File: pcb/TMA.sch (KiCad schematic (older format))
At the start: 22 parts, among them J1 Conn_01x02, J2 Conn_01x06, SW1 SW_SPDT, U1 BMP280, U2 BMI160, U3 ATtiny1614-SS, U4 MIC5504-3.3YM5

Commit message: Pick components.
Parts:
- C1, C2, C3, C4, C5, C6, C7: footprint (none) -> Capacitor_SMD:C_0402_1005Metric
- D1: renamed from D?; footprint (none) -> Diode_SMD:D_0402_1005Metric
- D3, D4: footprint (none) -> LED_SMD:LED_0402_1005Metric
- J1: footprint (none) -> Connector_JST:JST_PH_B2B-PH-K_1x02_P2.00mm_Vertical
- J2: footprint (none) -> Connector_JST:JST_PH_B6B-PH-K_1x06_P2.00mm_Vertical
- R1, R2, R3, R4, R5: footprint (none) -> Resistor_SMD:R_0402_1005Metric
- SW1: footprint (none) -> Button_Switch_SMD:SW_SPDT_PCM12
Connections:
- net UPDI: now also D1.2 (A)
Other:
- moved on the sheet: D1
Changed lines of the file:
@@
 F 0 "C1" H 2092 3346 50  0000 L CNN
 F 1 "100nF" H 2092 3255 50  0000 L CNN
-F 2 "" H 2000 3300 50  0001 C CNN
+F 2 "Capacitor_SMD:C_0402_1005Metric" H 2000 3300 50  0001 C CNN
 F 3 "~" H 2000 3300 50  0001 C CNN
 	1    2000 3300
@@
 F 0 "C2" H 2242 1096 50  0000 L CNN
 F 1 "100nF" H 2242 1005 50  0000 L CNN
-F 2 "" H 2150 1050 50  0001 C CNN
+F 2 "Capacitor_SMD:C_0402_1005Metric" H 2150 1050 50  0001 C CNN
 F 3 "~" H 2150 1050 50  0001 C CNN
 	1    2150 1050
@@
 F 0 "J1" H 2818 775 50  0000 C CNN
 F 1 "Conn_01x02" H 2818 866 50  0000 C CNN
-F 2 "" H 2900 1100 50  0001 C CNN
+F 2 "Connector_JST:JST_PH_B2B-PH-K_1x02_P2.00mm_Vertical" H 2900 1100 50  0001 C CNN
 F 3 "~" H 2900 1100 50  0001 C CNN
 	1    2900 1100
@@
 F 0 "C3" H 2942 2796 50  0000 L CNN
 F 1 "100nF" H 2942 2705 50  0000 L CNN
-F 2 "" H 2850 2750 50  0001 C CNN
+F 2 "Capacitor_SMD:C_0402_1005Metric" H 2850 2750 50  0001 C CNN
 F 3 "~" H 2850 2750 50  0001 C CNN
 	1    2850 2750
@@
 F 0 "C4" H 3592 1296 50  0000 L CNN
 F 1 "4u7" H 3592 1205 50  0000 L CNN
-F 2 "" H 3500 1250 50  0001 C CNN
+F 2 "Capacitor_SMD:C_0402_1005Metric" H 3500 1250 50  0001 C CNN
 F 3 "~" H 3500 1250 50  0001 C CNN
 	1    3500 1250
@@
 F 0 "C5" H 4042 1296 50  0000 L CNN
 F 1 "100nF" H 4042 1205 50  0000 L CNN
-F 2 "" H 3950 1250 50  0001 C CNN
+F 2 "Capacitor_SMD:C_0402_1005Metric" H 3950 1250 50  0001 C CNN
 F 3 "~" H 3950 1250 50  0001 C CNN
 	1    3950 1250
@@
 $EndComp
 Connection ~ 3950 1000
-Wire Wire Line
-	3950 1000 4300 1000
 $Comp
 L power:GND #PWR09
@@
 F 0 "C6" H 5642 1296 50  0000 L CNN
 F 1 "4u7" H 5642 1205 50  0000 L CNN
-F 2 "" H 5550 1250 50  0001 C CNN
+F 2 "Capacitor_SMD:C_0402_1005Metric" H 5550 1250 50  0001 C CNN
 F 3 "~" H 5550 1250 50  0001 C CNN
 	1    5550 1250
@@
 F 0 "C7" H 6092 1296 50  0000 L CNN
 F 1 "100nF" H 6092 1205 50  0000 L CNN
-F 2 "" H 6000 1250 50  0001 C CNN
+F 2 "Capacitor_SMD:C_0402_1005Metric" H 6000 1250 50  0001 C CNN
 F 3 "~" H 6000 1250 50  0001 C CNN
 	1    6000 1250
@@
 Wire Wire Line
 	4750 1500 4750 1450
-Wire Wire Line
-	4300 1000 4300 1200
-Wire Wire Line
-	4300 1200 4350 1200
-Connection ~ 4300 1000
-Wire Wire Line
-	4300 1000 4350 1000
 $Comp
 L power:+3.3V #PWR010
@@
 F 0 "R1" V 7454 1050 50  0000 C CNN
 F 1 "5k" V 7545 1050 50  0000 C CNN
-F 2 "" H 7650 1050 50  0001 C CNN
+F 2 "Resistor_SMD:R_0402_1005Metric" H 7650 1050 50  0001 C CNN
 F 3 "~" H 7650 1050 50  0001 C CNN
 	1    7650 1050
@@
 F 0 "J2" H 6868 725 50  0000 C CNN
 F 1 "Conn_01x06" H 6868 816 50  0000 C CNN
-F 2 "" H 6950 1250 50  0001 C CNN
+F 2 "Connector_JST:JST_PH_B6B-PH-K_1x06_P2.00mm_Vertical" H 6950 1250 50  0001 C CNN
 F 3 "~" H 6950 1250 50  0001 C CNN
 	1    6950 1250
@@
 F 0 "D3" V 8696 1030 50  0000 R CNN
 F 1 "BLUE" V 8605 1030 50  0000 R CNN
-F 2 "" V 8650 1100 50  0001 C CNN
+F 2 "LED_SMD:LED_0402_1005Metric" V 8650 1100 50  0001 C CNN
 F 3 "~" V 8650 1100 50  0001 C CNN
 	1    8650 1100
@@
 F 0 "D4" V 9496 1030 50  0000 R CNN
 F 1 "RED" V 9405 1030 50  0000 R CNN
-F 2 "" V 9450 1100 50  0001 C CNN
+F 2 "LED_SMD:LED_0402_1005Metric" V 9450 1100 50  0001 C CNN
 F 3 "~" V 9450 1100 50  0001 C CNN
 	1    9450 1100
@@
 F 0 "R2" H 8500 1300 50  0000 C CNN
 F 1 "10k" H 8500 1400 50  0000 C CNN
-F 2 "" H 8650 1350 50  0001 C CNN
+F 2 "Resistor_SMD:R_0402_1005Metric" H 8650 1350 50  0001 C CNN
 F 3 "~" H 8650 1350 50  0001 C CNN
 	1    8650 1350
@@
 F 0 "R3" H 9300 1300 50  0000 C CNN
 F 1 "10k" H 9300 1400 50  0000 C CNN
-F 2 "" H 9450 1350 50  0001 C CNN
+F 2 "Resistor_SMD:R_0402_1005Metric" H 9450 1350 50  0001 C CNN
 F 3 "~" H 9450 1350 50  0001 C CNN
 	1    9450 1350
@@
 F 0 "R4" V 10400 900 50  0000 C CNN
 F 1 "10k" V 10400 1050 50  0000 C CNN
-F 2 "" H 10500 1000 50  0001 C CNN
+F 2 "Resistor_SMD:R_0402_1005Metric" H 10500 1000 50  0001 C CNN
 F 3 "~" H 10500 1000 50  0001 C CNN
 	1    10500 1000
@@
 F 0 "R5" V 10400 700 50  0000 C CNN
 F 1 "10k" V 10400 850 50  0000 C CNN
-F 2 "" H 10500 800 50  0001 C CNN
+F 2 "Resistor_SMD:R_0402_1005Metric" H 10500 800 50  0001 C CNN
 F 3 "~" H 10500 800 50  0001 C CNN
 	1    10500 800
@@
 F 0 "SW1" H 10350 1350 50  0000 C CNN
 F 1 "SW_SPDT" H 10350 1450 50  0000 C CNN
-F 2 "" H 10550 1600 50  0001 C CNN
+F 2 "Button_Switch_SMD:SW_SPDT_PCM12" H 10550 1600 50  0001 C CNN
 F 3 "~" H 10550 1600 50  0001 C CNN
 	1    10550 1600
@@
 MODE
 Wire Wire Line
-	7800 1050 8000 1050
+	7800 1050 7900 1050
 Wire Wire Line
 	10600 800  10700 800
@@
 Connection ~ 10700 800
 $Comp
-L power:+3.3V #PWR?
+L power:+3.3V #PWR0107
 U 1 1 607905AF
-P 7900 700
-F 0 "#PWR?" H 7900 550 50  0001 C CNN
-F 1 "+3.3V" H 8100 800 50  0000 C CNN
-F 2 "" H 7900 700 50  0001 C CNN
-F 3 "" H 7900 700 50  0001 C CNN
-	1    7900 700
-	1    0    0    -1
-$EndComp
-$Comp
-L Device:D_Schottky D?
+P 7900 650
+F 0 "#PWR0107" H 7900 500 50  0001 C CNN
+F 1 "+3.3V" H 8100 750 50  0000 C CNN
+F 2 "" H 7900 650 50  0001 C CNN
+F 3 "" H 7900 650 50  0001 C CNN
+	1    7900 650
+	1    0    0    -1
+$EndComp
+$Comp
+L Device:D_Schottky D1
 U 1 1 607905B5
-P 7900 900
-F 0 "D?" V 7800 1050 50  0000 C CNN
-F 1 "D_Schottky" V 7900 1200 50  0000 C CNN
-F 2 "" H 7900 900 50  0001 C CNN
-F 3 "~" H 7900 900 50  0001 C CNN
-	1    7900 900
-	0    1    1    0
-$EndComp
-Wire Wire Line
-	7900 750  7900 700
+P 7900 850
+F 0 "D1" V 7800 1000 50  0000 C CNN
+F 1 "D_Schottky" V 7900 1150 50  0000 C CNN
+F 2 "Diode_SMD:D_0402_1005Metric" H 7900 850 50  0001 C CNN
+F 3 "~" H 7900 850 50  0001 C CNN
+	1    7900 850
+	0    1    1    0
+$EndComp
+Wire Wire Line
+	7900 700  7900 650
 Wire Notes Line
 	5400 4650 5400 1850
@@
 Wire Wire Line
 	6000 1000 6100 1000
+Wire Wire Line
+	7900 1050 7900 1000
+Connection ~ 7900 1050
+Wire Wire Line
+	7900 1050 8000 1050
+Wire Wire Line
+	3950 1000 4300 1000
+Wire Wire Line
+	4350 1200 4300 1200
+Wire Wire Line
+	4300 1200 4300 1000
+Connection ~ 4300 1000
+Wire Wire Line
+	4300 1000 4350 1000
 $EndSCHEMATC

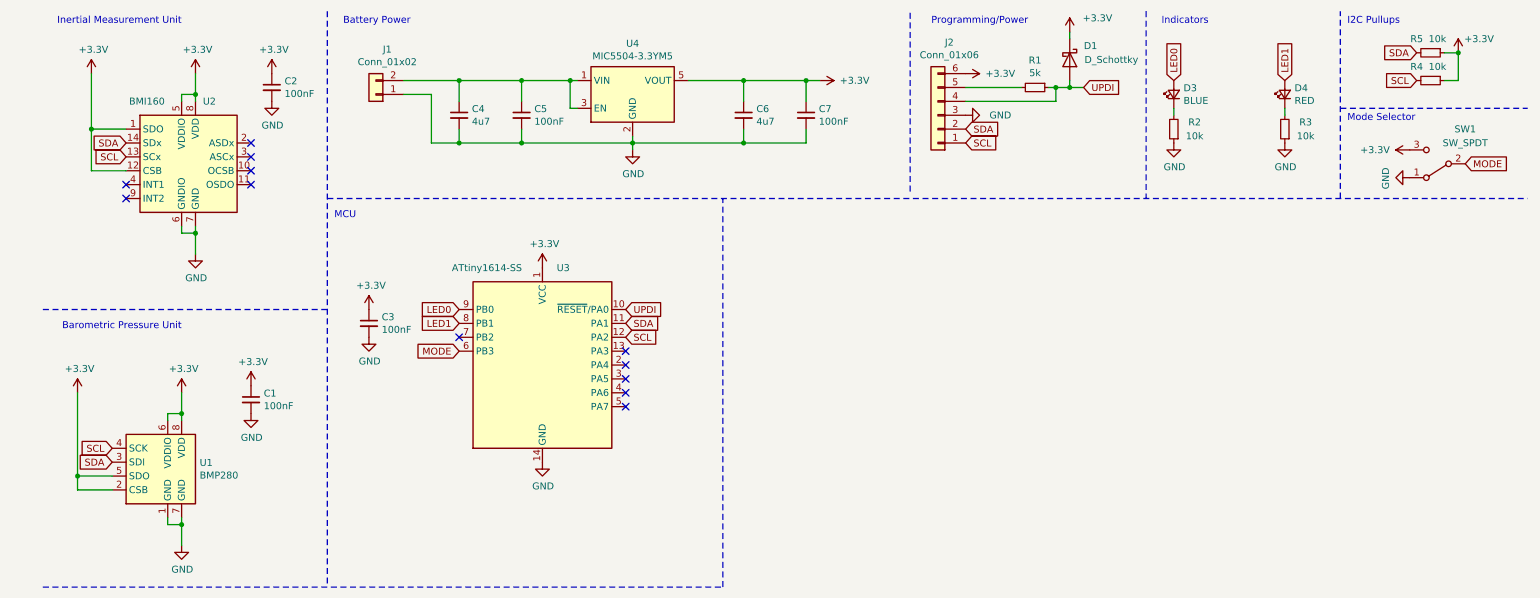
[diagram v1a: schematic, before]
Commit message: Serial, simplify programmer (trust it), break out I2C.
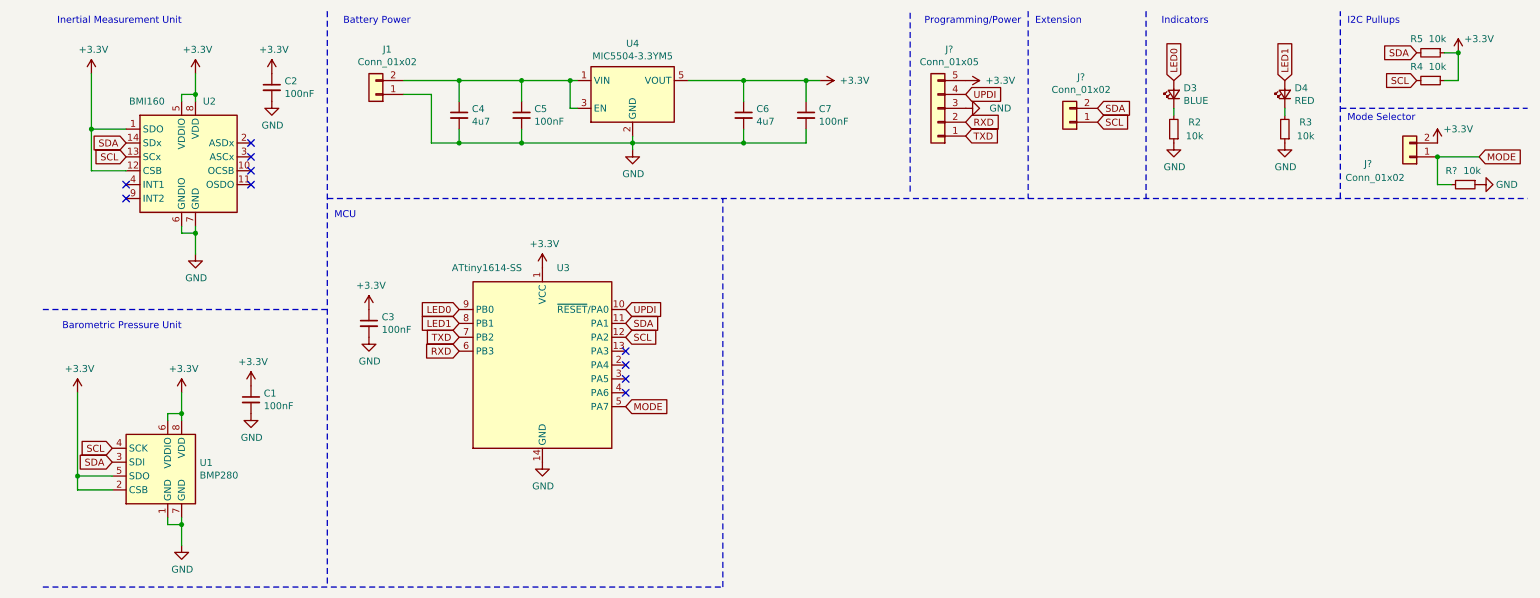
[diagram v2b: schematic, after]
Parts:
- removed D1: D_Schottky, Diode_SMD:D_0402_1005Metric, symbol Device:D_Schottky
- removed J2: Conn_01x06, Connector_JST:JST_PH_B6B-PH-K_1x06_P2.00mm_Vertical, symbol Connector_Generic:Conn_01x06
- removed R1: 5k, Resistor_SMD:R_0402_1005Metric, symbol Device:R_Small
- removed SW1: SW_SPDT, Button_Switch_SMD:SW_SPDT_PCM12, symbol Switch:SW_SPDT
- added J?: Conn_01x05, symbol Connector_Generic:Conn_01x05
- added J? (x2): Conn_01x02, symbol Connector_Generic:Conn_01x02
- added R?: 10k, Resistor_SMD:R_0402_1005Metric, symbol Device:R_Small
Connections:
- net +3V3: now also J?.2 (Pin_2), J?.5 (Pin_5)
- net GND: now also J?.3 (Pin_3), R?.1
- net MODE: now also U3.5 (PA7), J?.1 (Pin_1), R?.2; no longer U3.6 (PB3)
- net SCL: now also J?.1 (Pin_1)
- net SDA: now also J?.2 (Pin_2)
- net UPDI: now also J?.4 (Pin_4)
- net TXD: now reaches U3.7 (PB2)
- net TXD: now also J?.1 (Pin_1)
- new net RXD: J?.2 (Pin_2), U3.6 (PB3)
- no-connect marks 12 -> 10
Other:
- note added: "Extension"
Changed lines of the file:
@@
 Text Notes 3150 600  2    50   ~ 0
 Battery Power
-Text Notes 7600 600  2    50   ~ 0
+Text Notes 7550 600  2    50   ~ 0
 Programming/Power\n
 $Comp
@@
 L power:+3.3V #PWR011
 U 1 1 607C1119
-P 7150 950
-F 0 "#PWR011" H 7150 800 50  0001 C CNN
-F 1 "+3.3V" V 7150 1200 50  0000 C CNN
-F 2 "" H 7150 950 50  0001 C CNN
-F 3 "" H 7150 950 50  0001 C CNN
-	1    7150 950
+P 7150 1000
+F 0 "#PWR011" H 7150 850 50  0001 C CNN
+F 1 "+3.3V" V 7150 1250 50  0000 C CNN
+F 2 "" H 7150 1000 50  0001 C CNN
+F 3 "" H 7150 1000 50  0001 C CNN
+	1    7150 1000
 	0    1    1    0
 $EndComp
@@
 L power:GND #PWR012
 U 1 1 607C2610
-P 7150 1250
-F 0 "#PWR012" H 7150 1000 50  0001 C CNN
-F 1 "GND" V 7150 1000 50  0000 C CNN
-F 2 "" H 7150 1250 50  0001 C CNN
-F 3 "" H 7150 1250 50  0001 C CNN
-	1    7150 1250
+P 7150 1200
+F 0 "#PWR012" H 7150 950 50  0001 C CNN
+F 1 "GND" V 7150 950 50  0000 C CNN
+F 2 "" H 7150 1200 50  0001 C CNN
+F 3 "" H 7150 1200 50  0001 C CNN
+	1    7150 1200
 	0    -1   -1   0
 $EndComp
-$Comp
-L Device:R_Small R1
-U 1 1 607C634C
-P 7650 1050
-F 0 "R1" V 7454 1050 50  0000 C CNN
-F 1 "5k" V 7545 1050 50  0000 C CNN
-F 2 "Resistor_SMD:R_0402_1005Metric" H 7650 1050 50  0001 C CNN
-F 3 "~" H 7650 1050 50  0001 C CNN
-	1    7650 1050
-	0    1    1    0
-$EndComp
-Wire Wire Line
-	7150 1050 7550 1050
-Wire Wire Line
-	7800 1150 7800 1050
-Wire Wire Line
-	7800 1050 7750 1050
-Wire Wire Line
-	7150 1150 7800 1150
-Connection ~ 7800 1050
-Text GLabel 8000 1050 2    50   Input ~ 0
+Text GLabel 7150 1100 2    50   Input ~ 0
 UPDI
 Wire Notes Line
@@
 Text GLabel 4700 2850 2    50   Input ~ 0
 SCL
-$Comp
-L Connector_Generic:Conn_01x06 J2
-U 1 1 607F77F0
-P 6950 1250
-F 0 "J2" H 6868 725 50  0000 C CNN
-F 1 "Conn_01x06" H 6868 816 50  0000 C CNN
-F 2 "Connector_JST:JST_PH_B6B-PH-K_1x06_P2.00mm_Vertical" H 6950 1250 50  0001 C CNN
-F 3 "~" H 6950 1250 50  0001 C CNN
-	1    6950 1250
-	-1   0    0    1
-$EndComp
-Text GLabel 7150 1350 2    50   Input ~ 0
-SDA
-Text GLabel 7150 1450 2    50   Input ~ 0
-SCL
 NoConn ~ 4700 2950
 NoConn ~ 4700 3050
 NoConn ~ 4700 3150
 NoConn ~ 4700 3250
-NoConn ~ 4700 3350
 $Comp
 L Device:LED_Small D3
@@
 Text GLabel 3500 2750 0    50   Input ~ 0
 LED1
-NoConn ~ 3500 2850
 Text GLabel 8650 1000 1    50   Input ~ 0
 LED0
@@
 Text GLabel 10400 800  0    50   Input ~ 0
 SDA
+Text Notes 9900 600  0    50   ~ 0
+I2C Pullups\n
+Wire Notes Line
+	9850 1200 11200 1200
+Text GLabel 4700 3350 2    50   Input ~ 0
+MODE
+Wire Wire Line
+	10600 800  10700 800
+Wire Wire Line
+	10700 1000 10700 800
+Wire Wire Line
+	10600 1000 10700 1000
+Connection ~ 10700 800
+Wire Notes Line
+	5400 4650 5400 1850
+Wire Notes Line
+	500  4650 5400 4650
+Wire Notes Line
+	6750 1800 6750 500
+Wire Wire Line
+	6000 1000 6100 1000
+Wire Wire Line
+	3950 1000 4300 1000
+Wire Wire Line
+	4350 1200 4300 1200
+Wire Wire Line
+	4300 1200 4300 1000
+Connection ~ 4300 1000
+Wire Wire Line
+	4300 1000 4350 1000
+$Comp
+L Connector_Generic:Conn_01x05 J?
+U 1 1 607DB715
+P 6950 1200
+F 0 "J?" H 6868 775 50  0000 C CNN
+F 1 "Conn_01x05" H 6868 866 50  0000 C CNN
+F 2 "" H 6950 1200 50  0001 C CNN
+F 3 "~" H 6950 1200 50  0001 C CNN
+	1    6950 1200
+	-1   0    0    1
+$EndComp
+Text GLabel 3500 2950 0    50   Input ~ 0
+RXD
+Text GLabel 3500 2850 0    50   Input ~ 0
+TXD
+Text GLabel 7150 1300 2    50   Input ~ 0
+RXD
+Text GLabel 7150 1400 2    50   Input ~ 0
+TXD
+Wire Notes Line
+	7600 500  7600 1850
+Text Notes 7650 600  0    50   ~ 0
+Extension
+$Comp
+L Connector_Generic:Conn_01x02 J?
+U 1 1 607EE0F5
+P 7900 1300
+F 0 "J?" H 7818 975 50  0000 C CNN
+F 1 "Conn_01x02" H 7818 1066 50  0000 C CNN
+F 2 "" H 7900 1300 50  0001 C CNN
+F 3 "~" H 7900 1300 50  0001 C CNN
+	1    7900 1300
+	-1   0    0    1
+$EndComp
+Text GLabel 8100 1200 2    50   Input ~ 0
+SDA
+Text GLabel 8100 1300 2    50   Input ~ 0
+SCL
+Text GLabel 10850 1550 2    50   Input ~ 0
+MODE
+Text Notes 9900 1300 0    50   ~ 0
+Mode Selector
+$Comp
+L Connector_Generic:Conn_01x02 J?
+U 1 1 607F369F
+P 10350 1550
+F 0 "J?" H 10650 1600 50  0000 C CNN
+F 1 "Conn_01x02" H 10600 1700 50  0000 C CNN
+F 2 "" H 10350 1550 50  0001 C CNN
+F 3 "~" H 10350 1550 50  0001 C CNN
+	1    10350 1550
+	-1   0    0    1
+$EndComp
 $Comp
 L power:+3.3V #PWR017
@@
 	1    0    0    -1
 $EndComp
-Text Notes 9900 600  0    50   ~ 0
-I2C Pullups\n
-Wire Notes Line
-	9850 1200 11200 1200
-$Comp
-L Switch:SW_SPDT SW1
-U 1 1 60789BF3
-P 10550 1600
-F 0 "SW1" H 10350 1350 50  0000 C CNN
-F 1 "SW_SPDT" H 10350 1450 50  0000 C CNN
-F 2 "Button_Switch_SMD:SW_SPDT_PCM12" H 10550 1600 50  0001 C CNN
-F 3 "~" H 10550 1600 50  0001 C CNN
-	1    10550 1600
-	-1   0    0    1
-$EndComp
-Text GLabel 10750 1600 2    50   Input ~ 0
-MODE
-$Comp
-L power:+3.3V #PWR015
-U 1 1 6078E8D6
-P 10350 1500
-F 0 "#PWR015" H 10350 1350 50  0001 C CNN
-F 1 "+3.3V" V 10350 1750 50  0000 C CNN
-F 2 "" H 10350 1500 50  0001 C CNN
-F 3 "" H 10350 1500 50  0001 C CNN
-	1    10350 1500
+$Comp
+L power:+3.3V #PWR?
+U 1 1 607F6852
+P 10550 1450
+F 0 "#PWR?" H 10550 1300 50  0001 C CNN
+F 1 "+3.3V" H 10700 1550 50  0000 C CNN
+F 2 "" H 10550 1450 50  0001 C CNN
+F 3 "" H 10550 1450 50  0001 C CNN
+	1    10550 1450
+	1    0    0    -1
+$EndComp
+$Comp
+L Device:R_Small R?
+U 1 1 607F6F0C
+P 10750 1750
+F 0 "R?" V 10650 1650 50  0000 C CNN
+F 1 "10k" V 10650 1800 50  0000 C CNN
+F 2 "Resistor_SMD:R_0402_1005Metric" H 10750 1750 50  0001 C CNN
+F 3 "~" H 10750 1750 50  0001 C CNN
+	1    10750 1750
+	0    1    1    0
+$EndComp
+$Comp
+L power:GND #PWR?
+U 1 1 607F7A49
+P 10850 1750
+F 0 "#PWR?" H 10850 1500 50  0001 C CNN
+F 1 "GND" V 10850 1550 50  0000 C CNN
+F 2 "" H 10850 1750 50  0001 C CNN
+F 3 "" H 10850 1750 50  0001 C CNN
+	1    10850 1750
 	0    -1   -1   0
 $EndComp
-$Comp
-L power:GND #PWR016
-U 1 1 6078F1F6
-P 10350 1700
-F 0 "#PWR016" H 10350 1450 50  0001 C CNN
-F 1 "GND" H 10355 1527 50  0000 C CNN
-F 2 "" H 10350 1700 50  0001 C CNN
-F 3 "" H 10350 1700 50  0001 C CNN
-	1    10350 1700
-	0    1    1    0
-$EndComp
-Text Notes 9900 1300 0    50   ~ 0
-Mode Selector
-Text GLabel 3500 2950 0    50   Input ~ 0
-MODE
-Wire Wire Line
-	7800 1050 7900 1050
-Wire Wire Line
-	10600 800  10700 800
-Wire Wire Line
-	10700 1000 10700 800
-Wire Wire Line
-	10600 1000 10700 1000
-Connection ~ 10700 800
-$Comp
-L power:+3.3V #PWR0107
-U 1 1 607905AF
-P 7900 650
-F 0 "#PWR0107" H 7900 500 50  0001 C CNN
-F 1 "+3.3V" H 8100 750 50  0000 C CNN
-F 2 "" H 7900 650 50  0001 C CNN
-F 3 "" H 7900 650 50  0001 C CNN
-	1    7900 650
-	1    0    0    -1
-$EndComp
-$Comp
-L Device:D_Schottky D1
-U 1 1 607905B5
-P 7900 850
-F 0 "D1" V 7800 1000 50  0000 C CNN
-F 1 "D_Schottky" V 7900 1150 50  0000 C CNN
-F 2 "Diode_SMD:D_0402_1005Metric" H 7900 850 50  0001 C CNN
-F 3 "~" H 7900 850 50  0001 C CNN
-	1    7900 850
-	0    1    1    0
-$EndComp
-Wire Wire Line
-	7900 700  7900 650
-Wire Notes Line
-	5400 4650 5400 1850
-Wire Notes Line
-	500  4650 5400 4650
-Wire Notes Line
-	6750 1800 6750 500
-Wire Wire Line
-	6000 1000 6100 1000
-Wire Wire Line
-	7900 1050 7900 1000
-Connection ~ 7900 1050
-Wire Wire Line
-	7900 1050 8000 1050
-Wire Wire Line
-	3950 1000 4300 1000
-Wire Wire Line
-	4350 1200 4300 1200
-Wire Wire Line
-	4300 1200 4300 1000
-Connection ~ 4300 1000
-Wire Wire Line
-	4300 1000 4350 1000
+Wire Wire Line
+	10550 1550 10550 1750
+Wire Wire Line
+	10550 1750 10650 1750
+Wire Wire Line
+	10550 1550 10850 1550
+Connection ~ 10550 1550
 $EndSCHEMATC
